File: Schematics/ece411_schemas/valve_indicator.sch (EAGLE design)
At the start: 83 parts, among them T1 2N2222, T2 2N2222, T3 2N2222, T4 2N2222, U1 AZ34063UMTR-G1, U2 AZ34063UMTR-G1, U3 STM32F042K6

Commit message: digikey --> digi-key
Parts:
- L1, L2: DIS DigiKey -> Digi-Key
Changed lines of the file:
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@@
 </pinmapping>
 </spice>
-<attribute name="DIS" value="DigiKey"/>
+<attribute name="DIS" value="Digi-Key"/>
 <attribute name="DPN" value="811-2101-ND
 "/>
@@
 </pinmapping>
 </spice>
-<attribute name="DIS" value="DigiKey"/>
+<attribute name="DIS" value="Digi-Key"/>
 <attribute name="DPN" value="811-2101-ND
 "/>

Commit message: fixed issues with board, updated BOM
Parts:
- removed BUZZER: BUZZER, pinhead:PINHD-1X2
- removed LED1: LED1, pinhead:PINHD-1X2
- removed LED2: LED2, pinhead:PINHD-1X2
- removed LED3: LED3, pinhead:PINHD-1X2
- removed T1, T2, T3, T4: 2N2222, transistor:-NPN-SOT23-EBC
- added JP1: LEDS, pinhead:PINHD-2X4
- added Q1, Q2, Q3, Q4: PMV45EN2R, Q-Nexperia-Nchannel-MOSFET-PMV45EN2R:PMV45EN2R
- added R15, R16, R17, R18: 10k, rcl:R-US_R0603
- BATT: DIS (none) -> Digi-Key; DPN (none) -> 900-0022232021-ND; MFR (none) -> Molex; MPN (none) -> 0022232021
- HES1, HES2, HES3, HES4, HES5, HES6, HES7, HES8, HES9, SM_STAT: DIS (none) -> Digi-Key; DPN (none) -> WM2701-ND; MFR (none) -> Molex; MPN (none) -> 0022112032
- L1: DIS Digi-Key -> DigiKey
- R10, R11, R12, R13: value NP -> 1k; DIS (none) -> Digi-Key; DPN (none) -> RMCF0603JJ1K00CT-ND; MFR (none) -> Stackpole Electronics Inc; MPN (none) -> RMCF0603JJ1K00
- SD_CARD: value SD_CARD -> SD; device pinhead:PINHD-1X8 -> pinhead:PINHD-1X6; DIS (none) -> Digi-Key; DPN (none) -> A33867-ND; MFR (none) -> TE Connectivity AMP Connectors; MPN (none) -> 5-103635-5
- U3: DIS (none) -> Digi-Key; DPN (none) -> 497-14647-ND; MFR (none) -> STMicroelectronics; MPN (none) -> STM32F042K6T6
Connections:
- net N$1 renamed UART_RX
- removed net N$25: LED2.2, T2.C
- removed net N$28: BUZZER.2, T4.C
- removed net N$31: R12.1, T3.E
- removed net N$33: LED3.2, T3.C
- new net CLK: SD_CARD.4, U3.PA5
- new net CS: SD_CARD.1, U3.PB1
- new net DI: SD_CARD.2, U3.PA7
- new net DO: SD_CARD.3, U3.PA6
- new net LED1: JP1.7, R10.2
- new net LED2: JP1.5, R11.2
- new net N$1: Q4.D, R13.1
- new net N$23: JP1.1, R13.2
- net +10V: now also JP1.2, JP1.4, JP1.6, JP1.8; no longer BUZZER.1, LED1.1, LED2.1, LED3.1
- net +3V3: now also SD_CARD.6; no longer SD_CARD.2
- net GND: now also Q1.S, Q2.S, Q3.S, Q4.S, R15.1, R16.1, R17.1, R18.1, SD_CARD.5; no longer R10.2, R11.2, R12.2, R13.2, SD_CARD.4
- net N$10: now also JP1.3, R12.2; no longer LED1.2, T1.C
- net N$11: now also U3.PA11; no longer U3.PA5
- net N$12: now also C7.1, HES7.3, R7.2, U3.PA15; no longer C6.1, HES6.3, R6.2, U3.PA6
- net N$13: now also Q3.D, R12.1; no longer C7.1, HES7.3, R7.2, U3.PA7
- net N$22: now also Q1.G, R15.2; no longer T1.B
- net N$24: now also Q3.G, R17.2; no longer T3.B
- net N$26: now also Q1.D; no longer T1.E
- net N$27: now also Q2.D; no longer T2.E
- net N$29: now also C6.1, HES6.3, R6.2, U3.PA12; no longer R13.1, T4.E
- net N$34: now also Q4.G, R18.2; no longer T4.B
- net N$35: now also Q2.G, R16.2; no longer T2.B
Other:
- note added: "Indication Outputs, -3 LED arrays -1 Buzzer -SD Card Data Backup"
- note removed: "Indication Outputs, -3 LED arrays -1 Buzzer -1 SD Card Backup (strech goal)"
- note removed: "SD Card Data Backup (stretch goal)"
- moved on the sheet: R10, R11, R12, R13

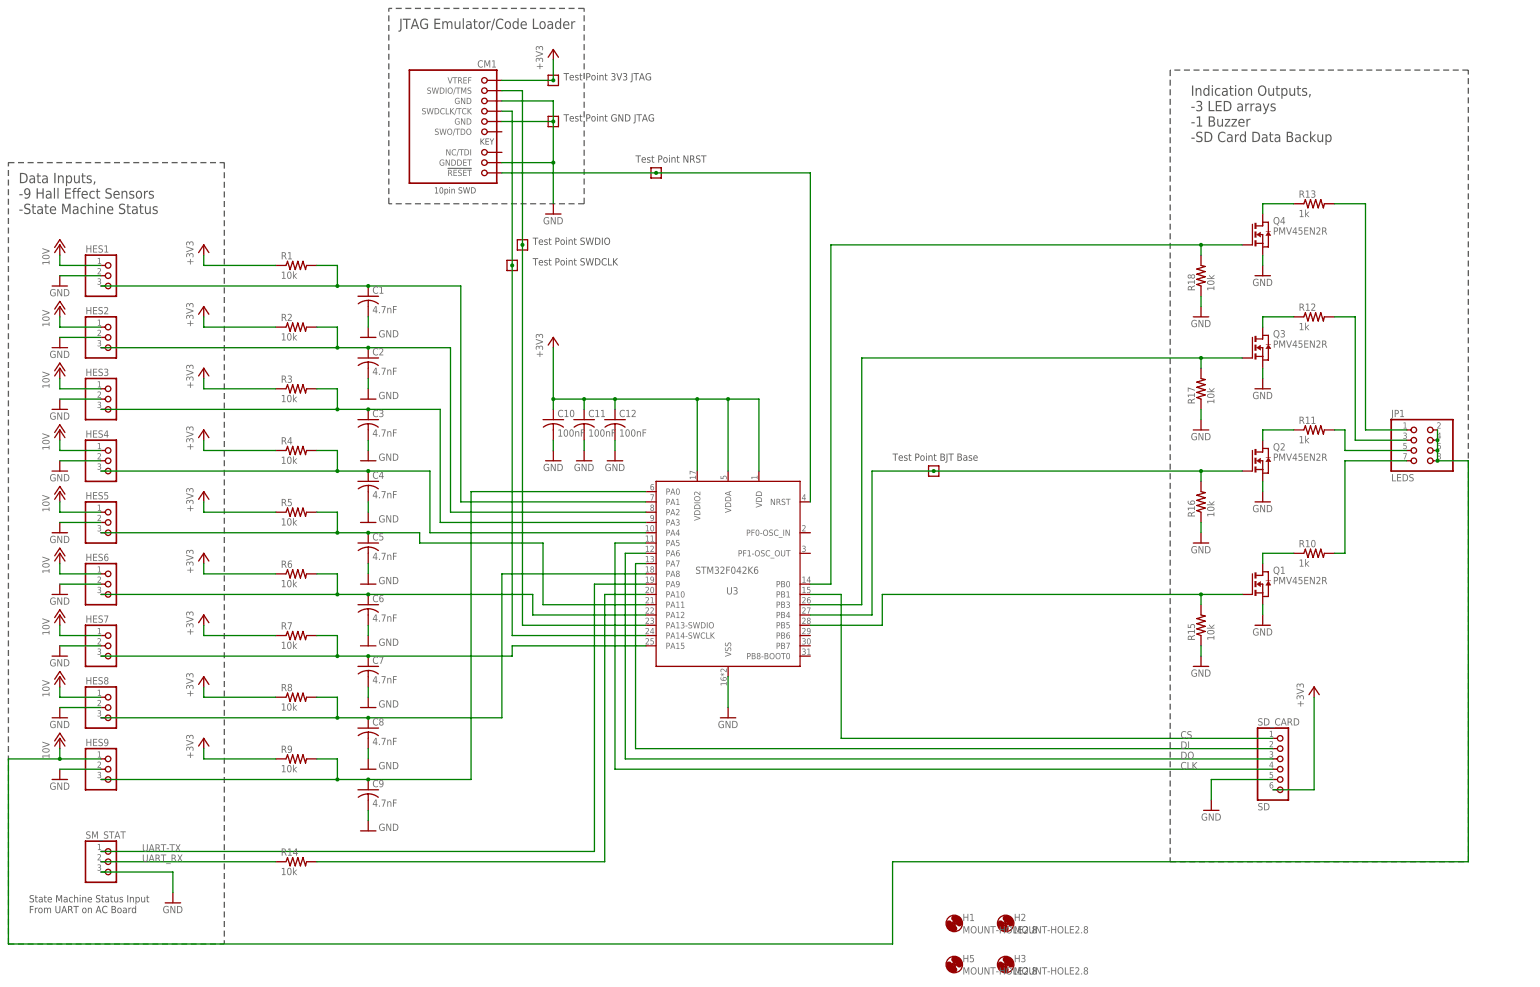
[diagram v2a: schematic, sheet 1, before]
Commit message: updated power lines
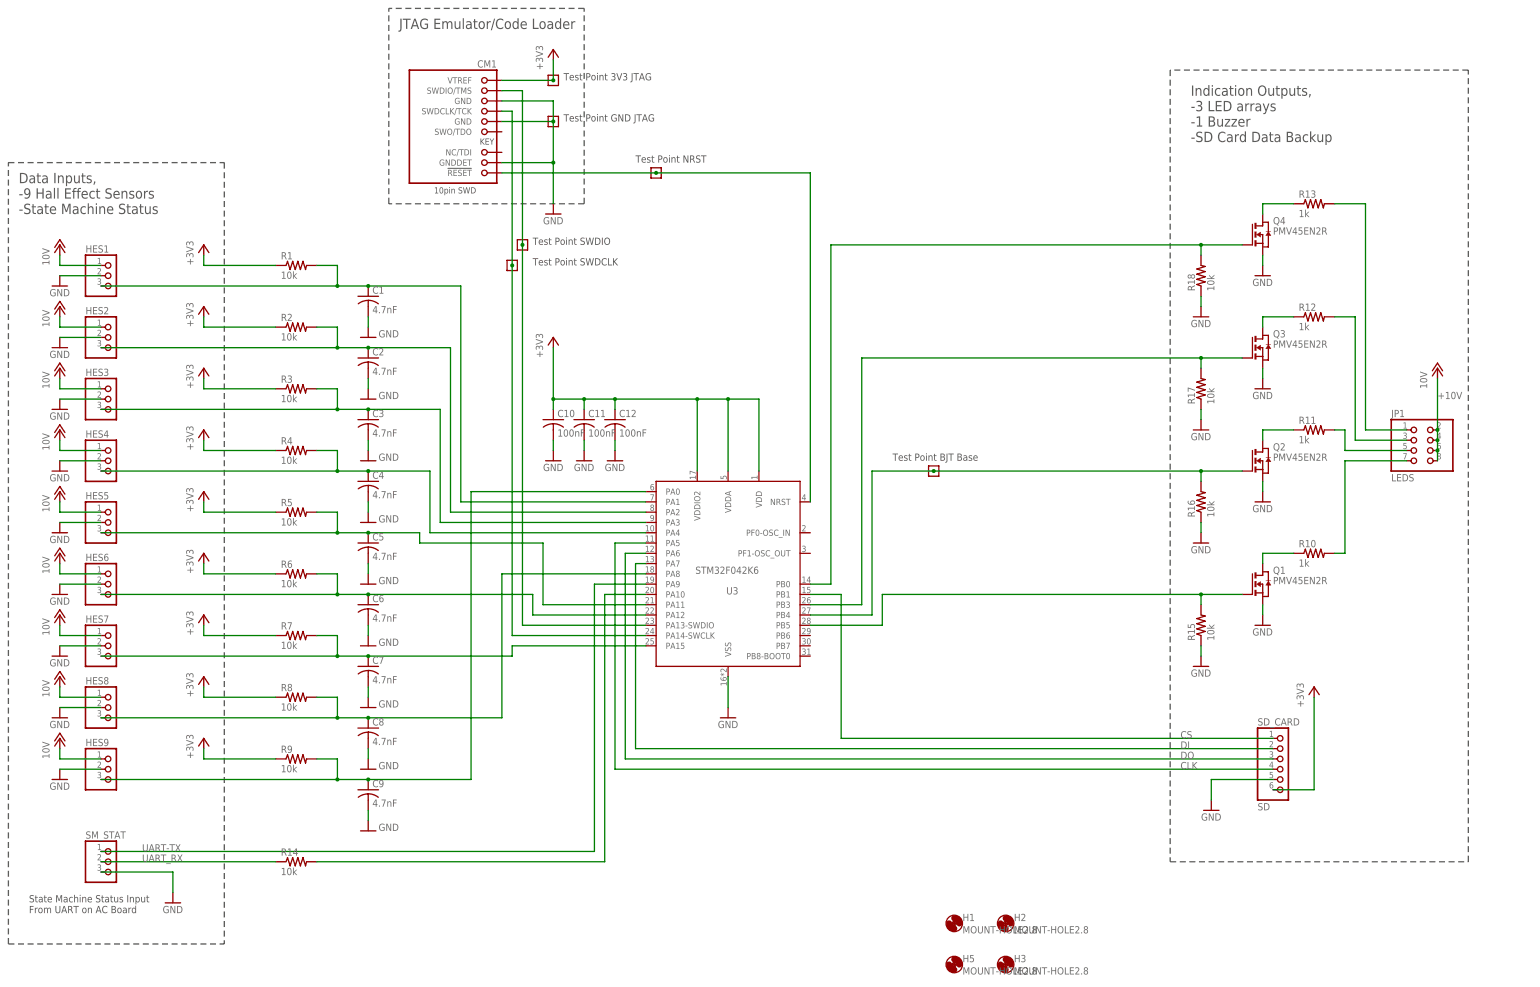
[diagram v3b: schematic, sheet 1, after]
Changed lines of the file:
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@@
 </part>
 <part name="JP1" library="pinhead" library_urn="urn:adsk.eagle:library:325" deviceset="PINHD-2X4" device="" package3d_urn="urn:adsk.eagle:package:22461/2" value="LEDS"/>
+<part name="P+1" library="supply1" library_urn="urn:adsk.eagle:library:371" deviceset="+12V" device="" value="10V"/>
 </parts>
 <sheets>
@@
 <attribute name="VALUE" x="354.33" y="129.54" size="1.778" layer="96"/>
 </instance>
+<instance part="P+1" gate="1" x="365.76" y="157.48" smashed="yes">
+<attribute name="VALUE" x="363.22" y="152.4" size="1.778" layer="96" rot="R90"/>
+</instance>
 </instances>
 <busses>
@@
 <wire x1="25.4" y1="60.96" x2="35.56" y2="60.96" width="0.1524" layer="91"/>
 <pinref part="P+4" gate="1" pin="+12V"/>
-<wire x1="25.4" y1="60.96" x2="12.7" y2="60.96" width="0.1524" layer="91"/>
-<wire x1="12.7" y1="60.96" x2="12.7" y2="15.24" width="0.1524" layer="91"/>
-<junction x="25.4" y="60.96"/>
-<pinref part="JP1" gate="A" pin="8"/>
-<pinref part="JP1" gate="A" pin="6"/>
-<wire x1="365.76" y1="134.62" x2="365.76" y2="137.16" width="0.1524" layer="91"/>
-<pinref part="JP1" gate="A" pin="4"/>
-<wire x1="365.76" y1="137.16" x2="365.76" y2="139.7" width="0.1524" layer="91"/>
-<junction x="365.76" y="137.16"/>
-<pinref part="JP1" gate="A" pin="2"/>
-<wire x1="365.76" y1="139.7" x2="365.76" y2="142.24" width="0.1524" layer="91"/>
-<junction x="365.76" y="139.7"/>
-<wire x1="12.7" y1="15.24" x2="231.14" y2="15.24" width="0.1524" layer="91"/>
-<junction x="365.76" y="134.62"/>
-<wire x1="373.38" y1="35.56" x2="231.14" y2="35.56" width="0.1524" layer="91"/>
-<wire x1="231.14" y1="35.56" x2="231.14" y2="15.24" width="0.1524" layer="91"/>
-<wire x1="373.38" y1="35.56" x2="373.38" y2="134.62" width="0.1524" layer="91"/>
-<wire x1="373.38" y1="134.62" x2="365.76" y2="134.62" width="0.1524" layer="91"/>
 </segment>
 <segment>
@@
 <pinref part="P+3" gate="1" pin="+12V"/>
 </segment>
-</net>
+<segment>
+<pinref part="P+1" gate="1" pin="+12V"/>
+<pinref part="JP1" gate="A" pin="2"/>
+<pinref part="JP1" gate="A" pin="4"/>
+<pinref part="JP1" gate="A" pin="6"/>
+<pinref part="JP1" gate="A" pin="8"/>
+<wire x1="365.76" y1="134.62" x2="365.76" y2="137.16" width="0.1524" layer="91"/>
+<junction x="365.76" y="137.16"/>
+<wire x1="365.76" y1="137.16" x2="365.76" y2="139.7" width="0.1524" layer="91"/>
+<junction x="365.76" y="139.7"/>
+<wire x1="365.76" y1="139.7" x2="365.76" y2="142.24" width="0.1524" layer="91"/>
+<wire x1="365.76" y1="142.24" x2="365.76" y2="154.94" width="0.1524" layer="91"/>
+<junction x="365.76" y="142.24"/>
+<label x="365.76" y="149.86" size="1.778" layer="95"/>
+</segment>
+</net>

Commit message: fixed error on board
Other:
- note added: "POE+ Power Supply to 3.3 Hall Effect Sensor Power"
- note added: "Regulator 1: POE+ 24V to 3.3V"
- note removed: "POE+ Power Supply to 3.6 Hall Effect Sensor Power"
- note removed: "Regulator 1: POE+ 24V to 3.6V"
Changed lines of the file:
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@@
 <wire x1="340.36" y1="243.84" x2="340.36" y2="162.56" width="0.1524" layer="97" style="shortdash"/>
 <text x="50.8" y="236.22" size="2.54" layer="97">Regulator 1:
-POE+ 24V to 3.6V</text>
+POE+ 24V to 3.3V</text>
 <text x="292.1" y="218.44" size="1.778" layer="97">3V3 powers all Hall Effect Sensors (HES#)</text>
-<text x="50.8" y="231.14" size="1.778" layer="97">POE+ Power Supply to 3.6 Hall Effect Sensor Power</text>
+<text x="50.8" y="231.14" size="1.778" layer="97">POE+ Power Supply to 3.3 Hall Effect Sensor Power</text>
 <text x="78.74" y="109.22" size="1.778" layer="97">POE Connector
 24V, Up to 30W

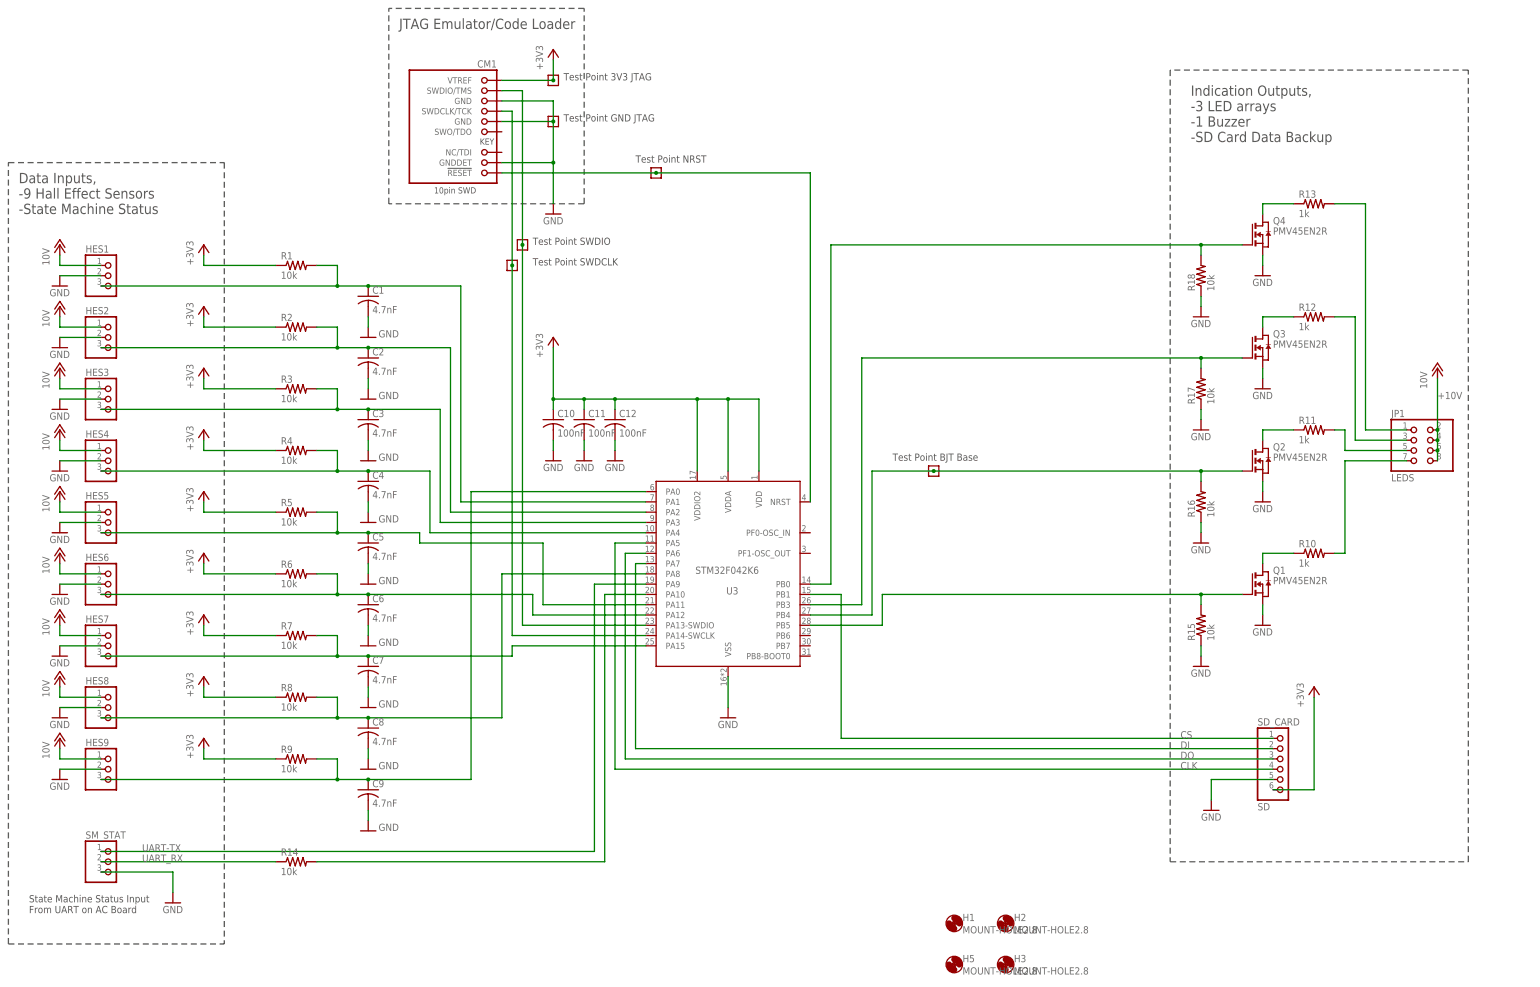
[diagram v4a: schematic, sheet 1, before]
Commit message: added cts/rts, cleanup, added backup pins
Added cts/rts to uart pin bus, cleaned up the schematic nets, and added pins for all the unused stm pins just in case.
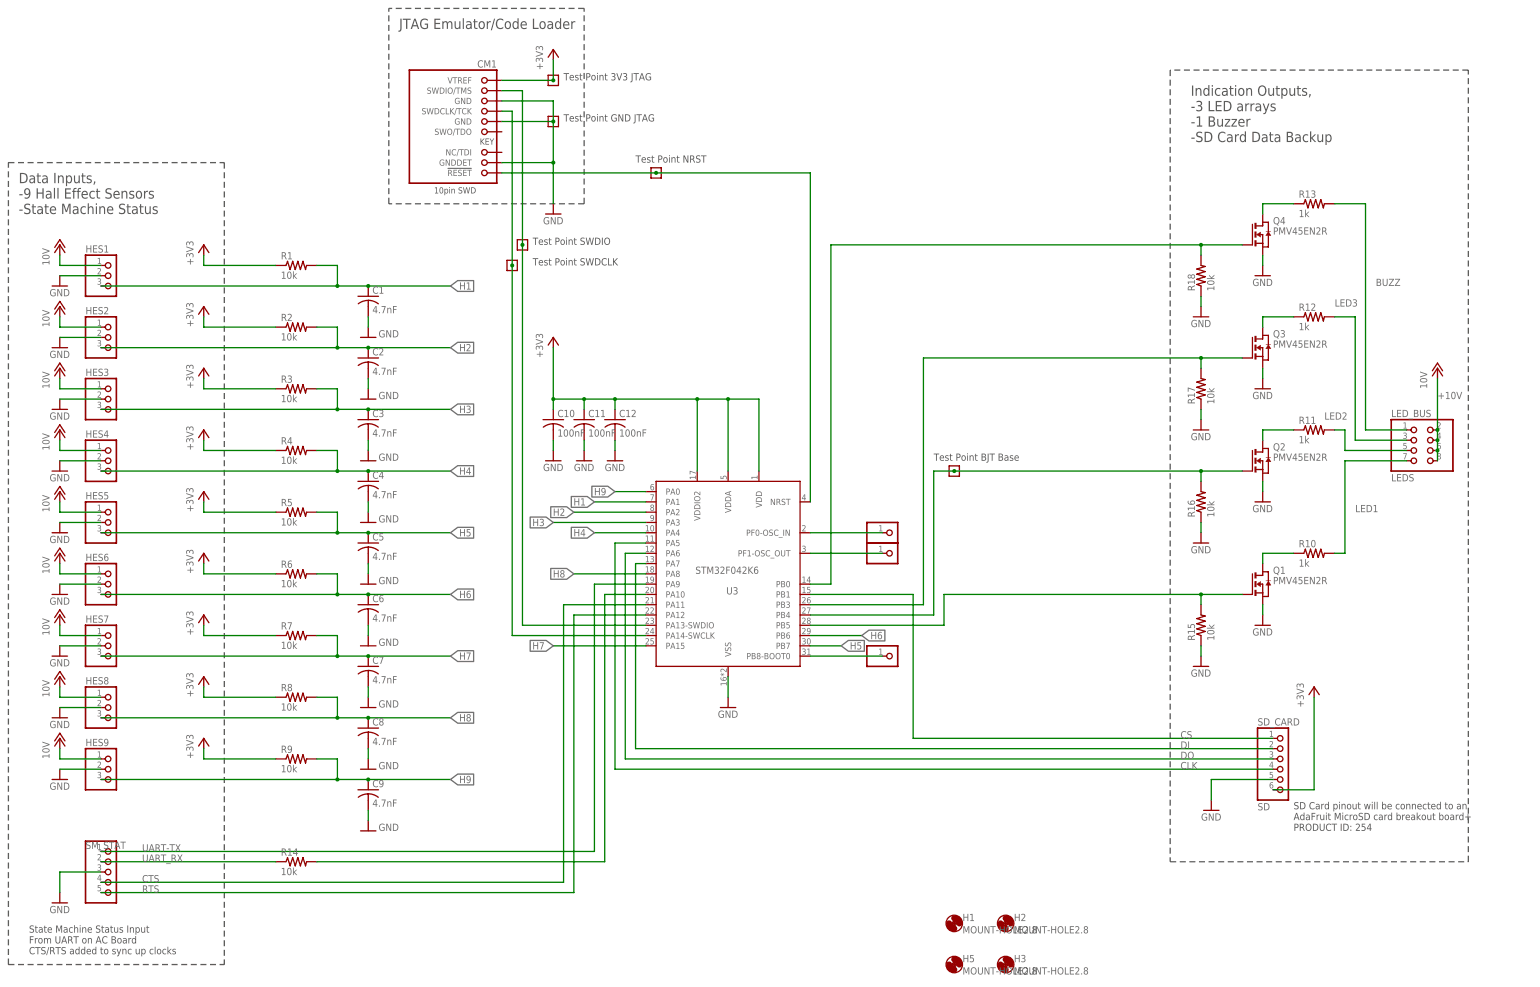
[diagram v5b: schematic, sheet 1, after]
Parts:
- added JP2: PF0-OSC_IN_PIN, pinhead:PINHD-1X1
- added JP3: PF1-OSC_OUT_PIN, pinhead:PINHD-1X1
- added JP4: PB8-BOOT0_PIN, pinhead:PINHD-1X1
- SM_STAT: device pinhead:PINHD-1X3 -> pinhead:PINHD-1X5
- renumbered JP1 to LED_BUS
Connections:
- net N$10 renamed LED3
- net N$12 renamed H7
- net N$14 renamed H8
- net N$15 renamed H9
- net N$17 renamed H4
- net N$23 renamed BUZZ
- net N$6 renamed H1
- net N$7 renamed H2
- net N$8 renamed H3
- removed net N$11: C5.1, HES5.3, R5.2, U3.PA11
- removed net N$29: C6.1, HES6.3, R6.2, U3.PA12
- new net CTS: SM_STAT.4, U3.PA11
- new net H5: C5.1, HES5.3, R5.2, U3.PB7
- new net H6: C6.1, HES6.3, R6.2, U3.PB6
- new net N$6: JP2.1, U3.PF0-OSC_IN
- new net N$7: JP3.1, U3.PF1-OSC_OUT
- new net N$8: JP4.1, U3.PB8-BOOT0
- new net RTS: SM_STAT.5, U3.PA12
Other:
- note added: "SD Card pinout will be connected to an AdaFruit MicroSD card breakout board+ PRODUCT ID: 254"
- note added: "State Machine Status Input From UART on AC Board CTS/RTS added to sync up clocks"
- note removed: "State Machine Status Input From UART on AC Board"

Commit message: corrections to board
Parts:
- C3_H, C3_L: device rcl:C-USC0603 -> rcl:C-US025-025X050
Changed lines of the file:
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@@
 <attribute name="MPN" value="0603B471K500CT"/>
 </part>
-<part name="C3_L" library="rcl" library_urn="urn:adsk.eagle:library:334" deviceset="C-US" device="C0603" package3d_urn="urn:adsk.eagle:package:23616/2" value="470uF">
+<part name="C3_L" library="rcl" library_urn="urn:adsk.eagle:library:334" deviceset="C-US" device="025-025X050" package3d_urn="urn:adsk.eagle:package:23629/2" value="470uF">
 <spice>
 <pinmapping spiceprefix="C">
@@
 <attribute name="MPN" value="ESH477M050AH4AA"/>
 </part>
-<part name="C3_H" library="rcl" library_urn="urn:adsk.eagle:library:334" deviceset="C-US" device="C0603" package3d_urn="urn:adsk.eagle:package:23616/2" value="470uF">
+<part name="C3_H" library="rcl" library_urn="urn:adsk.eagle:library:334" deviceset="C-US" device="025-025X050" package3d_urn="urn:adsk.eagle:package:23629/2" value="470uF">
 <spice>
 <pinmapping spiceprefix="C">
